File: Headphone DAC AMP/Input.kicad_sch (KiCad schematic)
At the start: 34 parts, among them J1 2137160001, J4 PINHD_1x2_Male, U2 XU316-1024-QF60B-C24, U8 W25Q16JVSNIQ

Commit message: Litterally didnt add anything because I spent an hour trying to understand how impedance matching works
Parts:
- added R18, R19: 22, Resistor_SMD:R_0805_2012Metric_Pad1.20x1.40mm_HandSolder, symbol Device:R
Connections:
- net D+: now also R18.1; no longer J1.A6 (DA+), J1.B6 (DB+)
- net D-: now also R19.1; no longer J1.A7 (DA-), J1.B7 (DB-)
- new net PRED+: J1.A6 (DA+), J1.B6 (DB+), R18.2
- new net PRED-: J1.A7 (DA-), J1.B7 (DB-), R19.2
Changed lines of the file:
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@@
 	(wire
 		(pts
+			(xy 46.99 76.2) (xy 49.53 76.2)
+		)
+		(stroke
+			(width 0)
+			(type default)
+		)
+	)
+	(wire
+		(pts
 			(xy 176.53 87.63) (xy 186.69 87.63)
 		)
@@
 	(wire
 		(pts
+			(xy 36.83 73.66) (xy 39.37 73.66)
+		)
+		(stroke
+			(width 0)
+			(type default)
+		)
+	)
+	(wire
+		(pts
 			(xy 167.64 17.78) (xy 177.8 17.78)
 		)
@@
 	(wire
 		(pts
-			(xy 242.57 100.33) (xy 252.73 100.33)
+			(xy 36.83 76.2) (xy 39.37 76.2)
 		)
 		(stroke
@@
 	(wire
 		(pts
-			(xy 71.12 26.67) (xy 90.17 26.67)
+			(xy 242.57 100.33) (xy 252.73 100.33)
 		)
 		(stroke
@@
 	(wire
 		(pts
-			(xy 260.35 16.51) (xy 250.19 16.51)
+			(xy 71.12 26.67) (xy 90.17 26.67)
 		)
 		(stroke
@@
 	(wire
 		(pts
-			(xy 219.71 16.51) (xy 219.71 19.05)
+			(xy 260.35 16.51) (xy 250.19 16.51)
 		)
 		(stroke
@@
 	(wire
 		(pts
-			(xy 134.62 167.64) (xy 134.62 170.18)
+			(xy 219.71 16.51) (xy 219.71 19.05)
 		)
 		(stroke
@@
 	(wire
 		(pts
-			(xy 176.53 74.93) (xy 186.69 74.93)
+			(xy 134.62 167.64) (xy 134.62 170.18)
 		)
 		(stroke
@@
 	(wire
 		(pts
-			(xy 46.99 73.66) (xy 49.53 73.66)
+			(xy 176.53 74.93) (xy 186.69 74.93)
 		)
 		(stroke
@@
 	(wire
 		(pts
-			(xy 46.99 76.2) (xy 49.53 76.2)
-		)
-		(stroke
-			(width 0)
-			(type default)
-		)
-	)
-	(wire
-		(pts
 			(xy 200.66 19.05) (xy 200.66 16.51)
 		)
@@
 	(wire
 		(pts
+			(xy 46.99 73.66) (xy 49.53 73.66)
+		)
+		(stroke
+			(width 0)
+			(type default)
+		)
+	)
+	(wire
+		(pts
 			(xy 229.87 16.51) (xy 229.87 19.05)
 		)
@@
 		)
 	)
-	(label "D+"
-		(at 46.99 73.66 0)
-		(effects
-			(font
-				(size 1.27 1.27)
-			)
-			(justify left bottom)
-		)
-	)
 	(label "QSPI_CLK"
 		(at 128.27 172.72 180)
@@
 		)
 	)
+	(label "D-"
+		(at 36.83 76.2 180)
+		(effects
+			(font
+				(size 1.27 1.27)
+			)
+			(justify right bottom)
+		)
+	)
 	(label "0V9BP"
 		(at 176.53 95.25 0)
@@
 		)
 	)
-	(label "D-"
-		(at 46.99 76.2 0)
+	(label "D+"
+		(at 168.91 138.43 180)
 		(effects
 			(font
 				(size 1.27 1.27)
 			)
-			(justify left bottom)
+			(justify right bottom)
 		)
 	)
-	(label "D+"
-		(at 168.91 138.43 180)
+	(label "PRED-"
+		(at 49.53 76.2 180)
 		(effects
 			(font
@@
 		)
 	)
+	(label "D+"
+		(at 36.83 73.66 180)
+		(effects
+			(font
+				(size 1.27 1.27)
+			)
+			(justify right bottom)
+		)
+	)
 	(label "D-"
 		(at 168.91 135.89 180)
@@
 		)
 	)
-	(label "D-"
+	(label "PRED+"
+		(at 49.53 73.66 180)
+		(effects
+			(font
+				(size 1.27 1.27)
+			)
+			(justify right bottom)
+		)
+	)
+	(label "PRED-"
 		(at 87.63 76.2 180)
 		(effects
@@
 		)
 	)
-	(label "D+"
+	(label "PRED+"
 		(at 87.63 73.66 180)
 		(effects
@@
 	)
 	(symbol
+		(lib_id "Device:R")
+		(at 43.18 76.2 90)
+		(unit 1)
+		(exclude_from_sim no)
+		(in_bom yes)
+		(on_board yes)
+		(dnp no)
+		(property "Reference" "R19"
+			(at 43.18 69.85 90)
+			(effects
+				(font
+					(size 1.27 1.27)
+				)
+			)
+		)
+		(property "Value" "22"
+			(at 43.18 72.136 90)
+			(effects
+				(font
+					(size 1.27 1.27)
+				)
+			)
+		)
+		(property "Footprint" "Resistor_SMD:R_0805_2012Metric_Pad1.20x1.40mm_HandSolder"
+			(at 43.18 77.978 90)
+			(effects
+				(font
+					(size 1.27 1.27)
+				)
+				(hide yes)
+			)
+		)
+		(property "Datasheet" "~"
+			(at 43.18 76.2 0)
+			(effects
+				(font
+					(size 1.27 1.27)
+				)
+				(hide yes)
+			)
+		)
+		(property "Description" "Resistor"
+			(at 43.18 76.2 0)
+			(effects
+				(font
+					(size 1.27 1.27)
+				)
+				(hide yes)
+			)
+		)
+		(pin "2"
+		)
+		(pin "1"
+		)
+		(instances
+			(project "Headphone DAC AMP"
+				(path "/d034eddd-efbc-47be-a25c-37cbfbab4cd8/2765e1cc-205a-4739-b769-20b95f3d1fdb"
+					(reference "R19")
+					(unit 1)
+				)
+			)
+		)
+	)
+	(symbol
 		(lib_id "power:GND")
 		(at 114.3 40.64 270)
@@
 					(unit 1)
 				)
+			)
+		)
+	)
+	(symbol
+		(lib_id "Device:R")
+		(at 43.18 73.66 90)
+		(unit 1)
+		(exclude_from_sim no)
+		(in_bom yes)
+		(on_board yes)
+		(dnp no)
+		(property "Reference" "R18"
+			(at 43.18 67.31 90)
+			(effects
+				(font
+					(size 1.27 1.27)
+				)
+			)
+		)
+		(property "Value" "22"
+			(at 43.18 69.088 90)
+			(effects
+				(font
+					(size 1.27 1.27)
+				)
+			)
+		)
+		(property "Footprint" "Resistor_SMD:R_0805_2012Metric_Pad1.20x1.40mm_HandSolder"
+			(at 43.18 75.438 90)
+			(effects
+				(font
+					(size 1.27 1.27)
+				)
+				(hide yes)
+			)
+		)
+		(property "Datasheet" "~"
+			(at 43.18 73.66 0)
+			(effects
+				(font
+					(size 1.27 1.27)
+				)
+				(hide yes)
+			)
+		)
+		(property "Description" "Resistor"
+			(at 43.18 73.66 0)
+			(effects
+				(font
+					(size 1.27 1.27)
+				)
+				(hide yes)
+			)
+		)
+		(pin "2"
+		)
+		(pin "1"
+		)
+		(instances
+			(project ""
+				(path "/d034eddd-efbc-47be-a25c-37cbfbab4cd8/2765e1cc-205a-4739-b769-20b95f3d1fdb"
+					(reference "R18")
+					(unit 1)
+				)

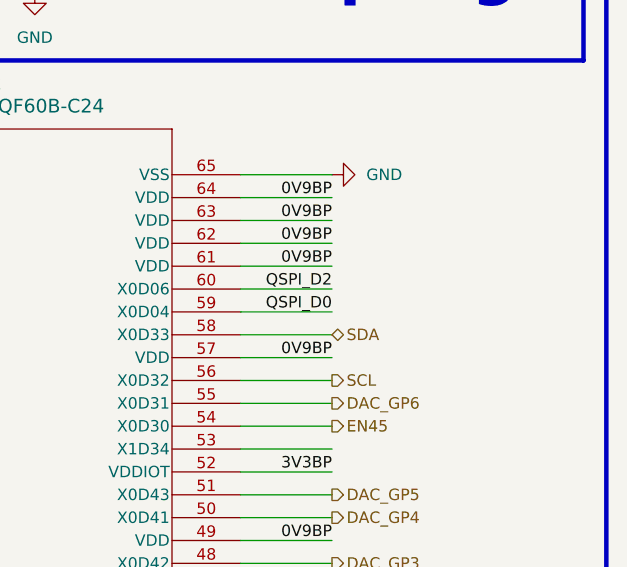
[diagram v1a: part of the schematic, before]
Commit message: Added I2C Pullups
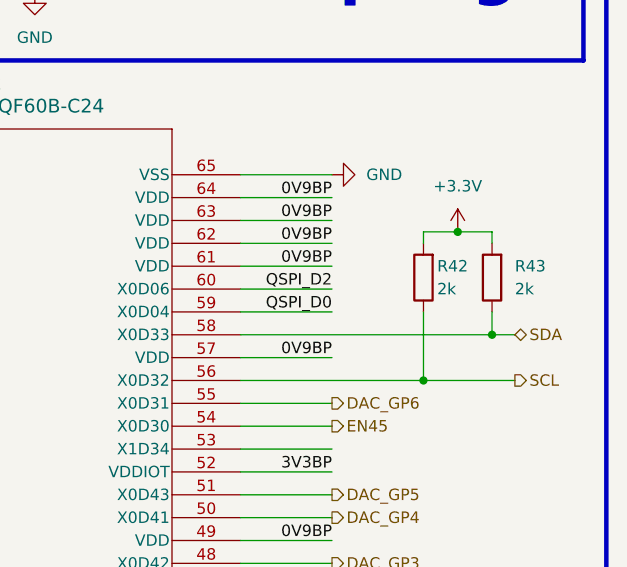
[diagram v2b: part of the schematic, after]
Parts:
- added R42, R43: 2k, Resistor_SMD:R_0805_2012Metric_Pad1.20x1.40mm_HandSolder, symbol Device:R
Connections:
- net +3.3V: now also R42.2, R43.2
- net SCL: now also R42.1
- net SDA: now also R43.1

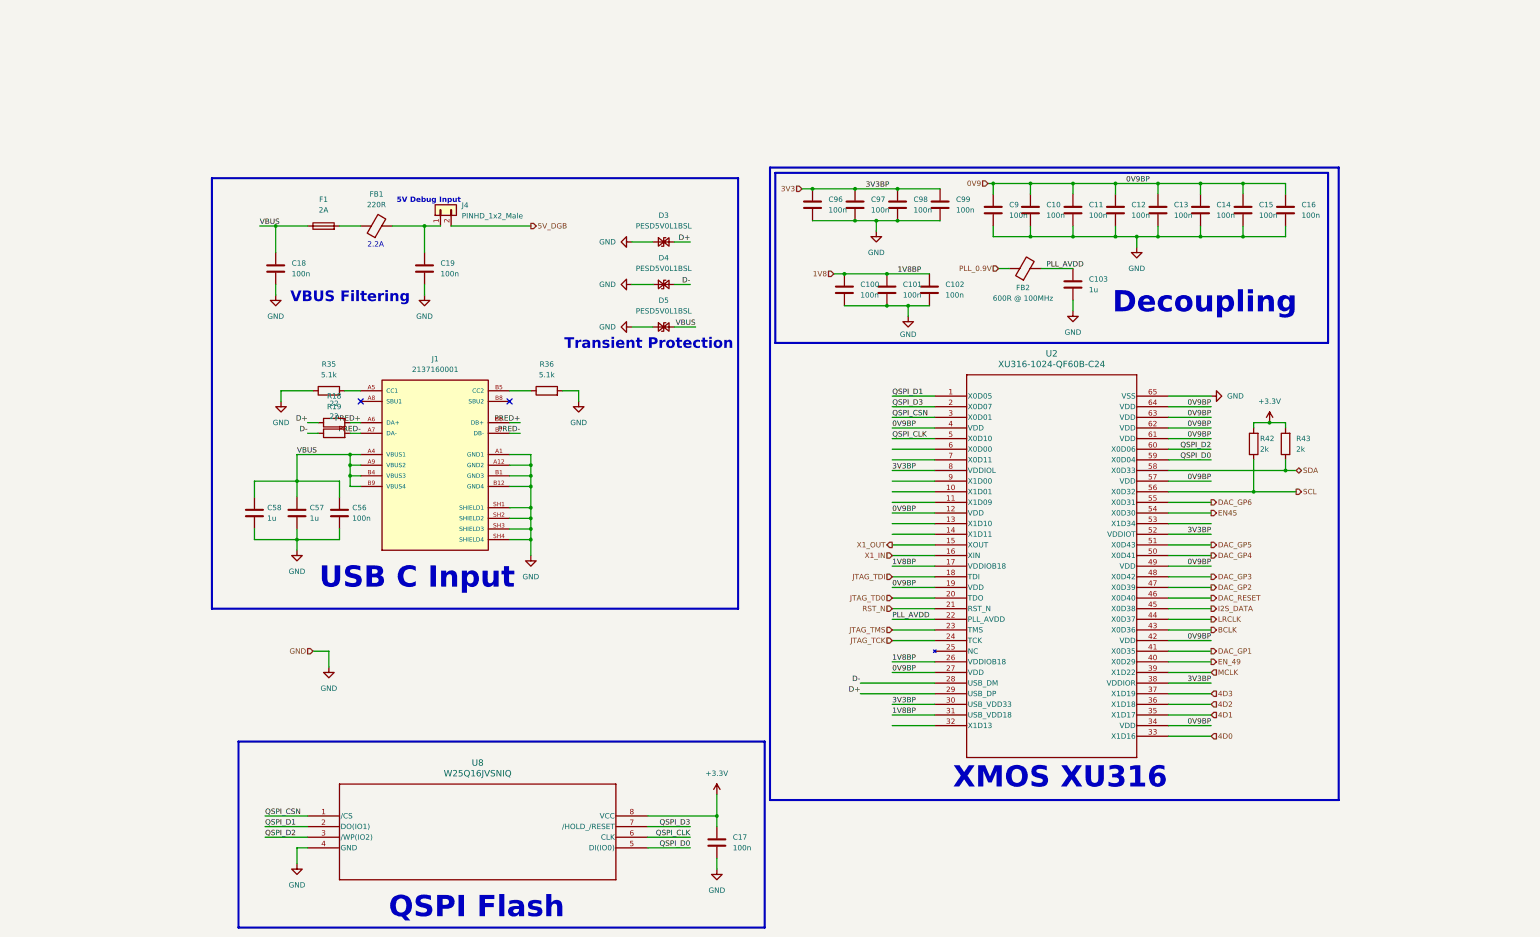
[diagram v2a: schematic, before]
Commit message: (Post Board Order) updated BOM with component links
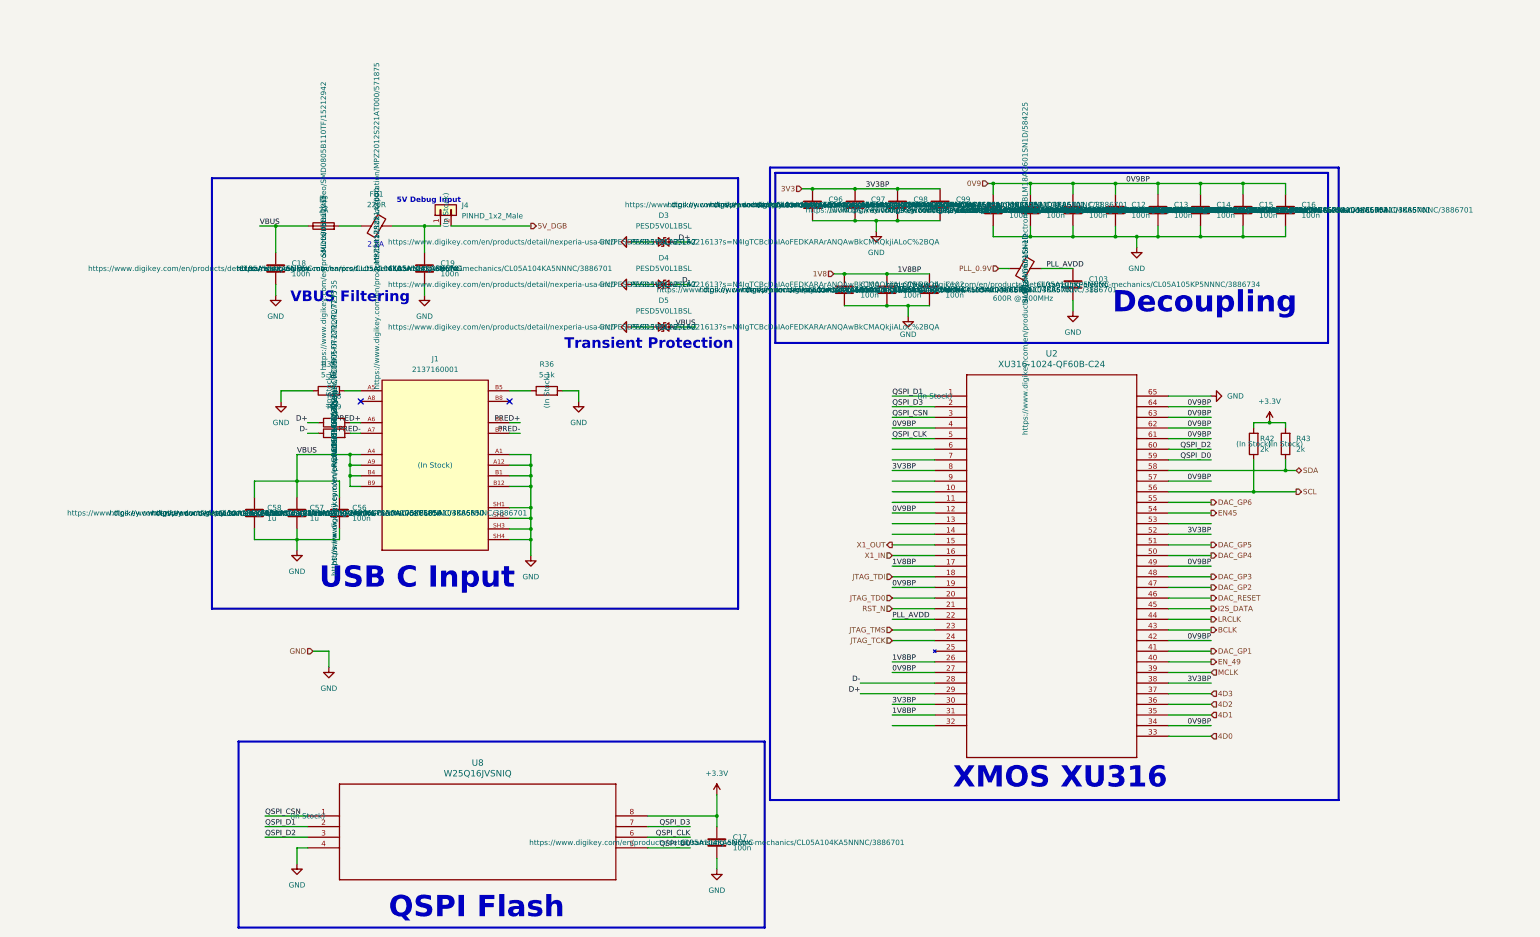
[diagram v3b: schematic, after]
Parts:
- C10, C100, C101, C102, C11, C12, C13, C14, C15, C16, C17, C18, C19, C56, C9, C96, C97, C98, C99: CUI_PURCHASE_URL (none) -> https://www.digikey.com/en/products/detail/samsung-electro-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; Mouser Part Number (none) -> CL05A104KA5NNNC
- C103: CUI_PURCHASE_URL (none) -> https://www.digikey.com/en/products/detail/samsung-electro-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; Mouser Part Number (none) -> CL05A105KP5NNNC
- C57, C58: CUI_PURCHASE_URL (none) -> https://www.digikey.com/en/products/detail/samsung-electro-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; Mouser Part Number (none) -> CL10A106KP8NNNC
- D3, D4, D5: CUI_PURCHASE_URL (none) -> https://www.digikey.com/en/products/detail/nexperia-usa-inc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; Mouser Part Number (none) -> PESD5V0L1BSLAZ
- F1: CUI_PURCHASE_URL (none) -> https://www.digikey.com/en/products/detail/yageo/SMD0805B11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; Mouser Part Number (none) -> SMD0805B110TF
- FB1: CUI_PURCHASE_URL (none) -> https://www.digikey.com/en/products/detail/tdk-corporation/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; Mouser Part Number (none) -> MPZ2012S221AT000
- FB2: CUI_PURCHASE_URL (none) -> https://www.digikey.com/en/products/detail/murata-electroni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; Mouser Part Number (none) -> BLM18AG601SN1D
- J1, J4, R35, R36, R42, R43, U2, U8: CUI_PURCHASE_URL (none) -> (In Stock)
- R18, R19: CUI_PURCHASE_URL (none) -> https://www.digikey.com/en/products/detail/yageo/RC0805FR-0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; Mouser Part Number (none) -> RC0805FR-0722RL
